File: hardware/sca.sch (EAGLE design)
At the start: 38 parts

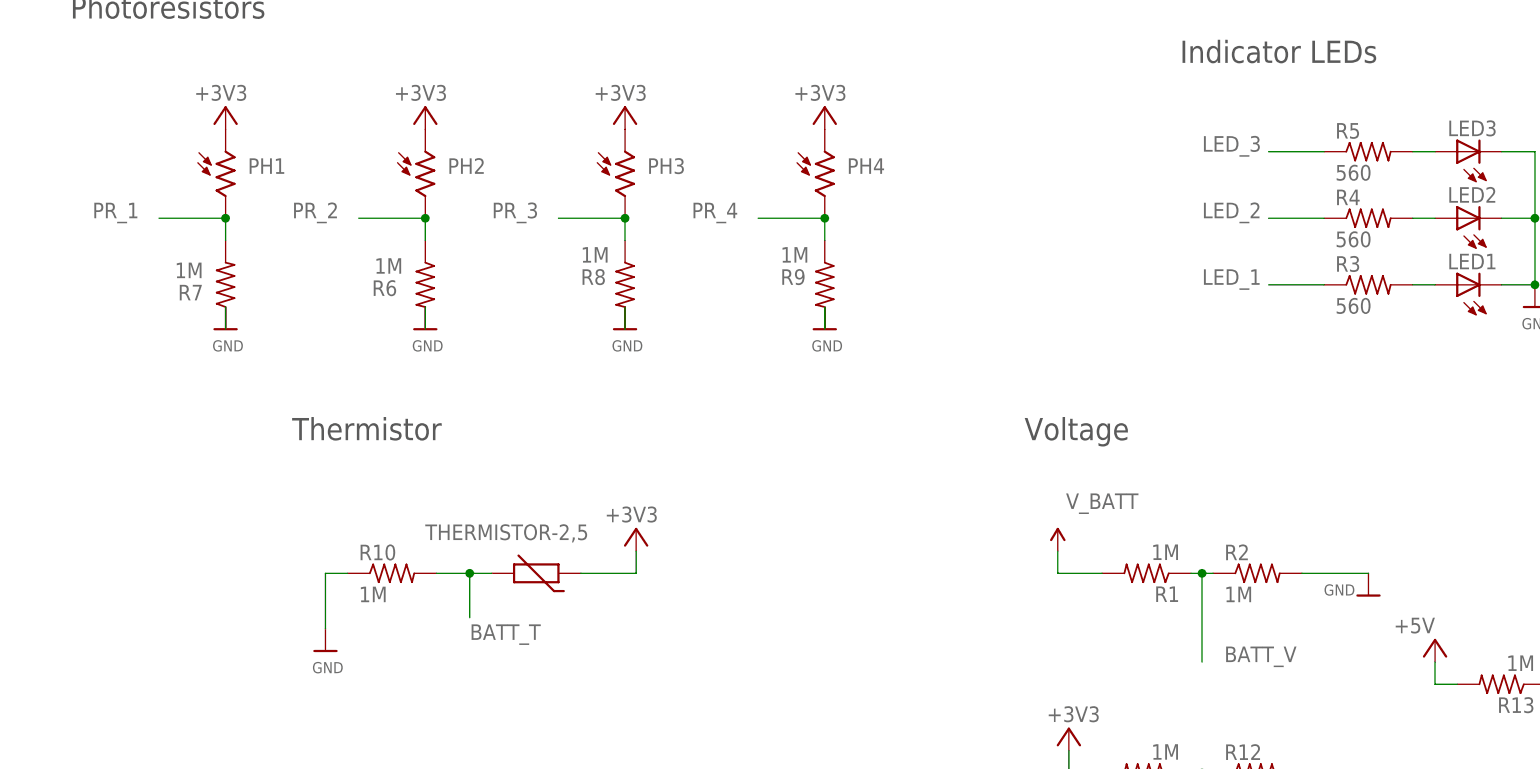
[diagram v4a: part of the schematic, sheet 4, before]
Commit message: updated resistor values
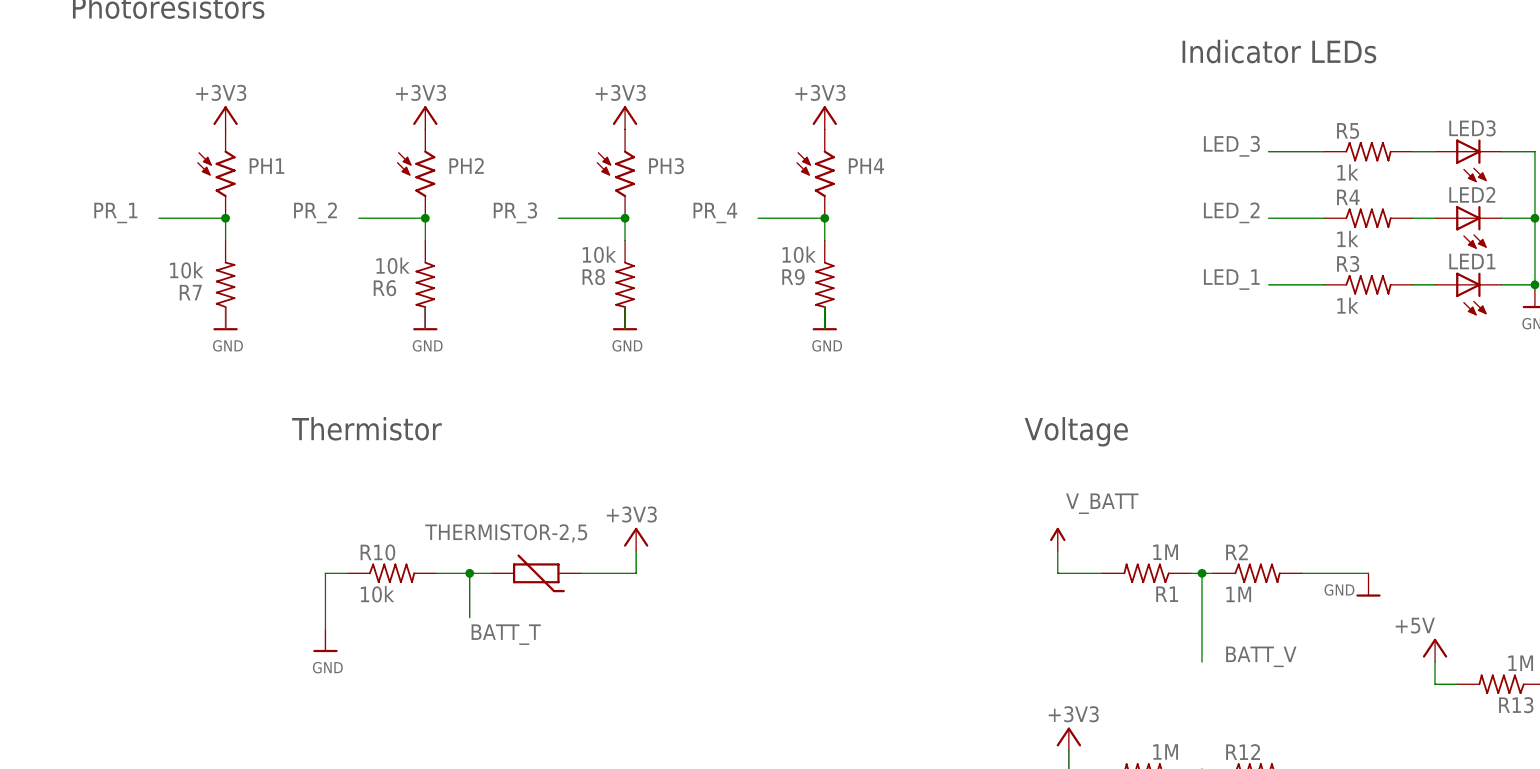
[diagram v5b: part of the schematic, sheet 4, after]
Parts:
- R10, R6, R7, R8, R9: value 1M -> 10k
- R3, R4, R5: value 560 -> 1k
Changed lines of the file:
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@@
 <part name="GPS_H" library="microbuilder" deviceset="HEADER-1X9" device="70MIL"/>
 <part name="P+8" library="supply1" deviceset="+5V" device=""/>
-<part name="R3" library="resistor" library_urn="urn:adsk.eagle:library:348" deviceset="R-US_" device="0309/10" package3d_urn="urn:adsk.eagle:package:23567/1" value="560"/>
-<part name="R4" library="resistor" library_urn="urn:adsk.eagle:library:348" deviceset="R-US_" device="0309/10" package3d_urn="urn:adsk.eagle:package:23567/1" value="560"/>
+<part name="R3" library="resistor" library_urn="urn:adsk.eagle:library:348" deviceset="R-US_" device="0309/10" package3d_urn="urn:adsk.eagle:package:23567/1" value="1k"/>
+<part name="R4" library="resistor" library_urn="urn:adsk.eagle:library:348" deviceset="R-US_" device="0309/10" package3d_urn="urn:adsk.eagle:package:23567/1" value="1k"/>
 <part name="LED1" library="adafruit" library_urn="urn:adsk.eagle:library:420" deviceset="LED" device="3MM" package3d_urn="urn:adsk.eagle:package:6240537/1"/>
 <part name="LED2" library="adafruit" library_urn="urn:adsk.eagle:library:420" deviceset="LED" device="3MM" package3d_urn="urn:adsk.eagle:package:6240537/1"/>
 <part name="LED3" library="adafruit" library_urn="urn:adsk.eagle:library:420" deviceset="LED" device="3MM" package3d_urn="urn:adsk.eagle:package:6240537/1"/>
-<part name="R5" library="resistor" library_urn="urn:adsk.eagle:library:348" deviceset="R-US_" device="0309/10" package3d_urn="urn:adsk.eagle:package:23567/1" value="560"/>
+<part name="R5" library="resistor" library_urn="urn:adsk.eagle:library:348" deviceset="R-US_" device="0309/10" package3d_urn="urn:adsk.eagle:package:23567/1" value="1k"/>
 <part name="U$2" library="microbuilder" deviceset="GND" device=""/>
 <part name="R1" library="resistor" library_urn="urn:adsk.eagle:library:348" deviceset="R-US_" device="0309/10" package3d_urn="urn:adsk.eagle:package:23567/1" value="1M"/>
@@
 <part name="+3V9" library="supply1" deviceset="+3V3" device=""/>
 <part name="+3V10" library="supply1" deviceset="+3V3" device=""/>
-<part name="R6" library="resistor" library_urn="urn:adsk.eagle:library:348" deviceset="R-US_" device="0309/10" package3d_urn="urn:adsk.eagle:package:23567/1" value="1M"/>
-<part name="R7" library="resistor" library_urn="urn:adsk.eagle:library:348" deviceset="R-US_" device="0309/10" package3d_urn="urn:adsk.eagle:package:23567/1" value="1M"/>
-<part name="R8" library="resistor" library_urn="urn:adsk.eagle:library:348" deviceset="R-US_" device="0309/10" package3d_urn="urn:adsk.eagle:package:23567/1" value="1M"/>
-<part name="R9" library="resistor" library_urn="urn:adsk.eagle:library:348" deviceset="R-US_" device="0309/10" package3d_urn="urn:adsk.eagle:package:23567/1" value="1M"/>
-<part name="R10" library="resistor" library_urn="urn:adsk.eagle:library:348" deviceset="R-US_" device="0309/10" package3d_urn="urn:adsk.eagle:package:23567/1" value="1M"/>
+<part name="R6" library="resistor" library_urn="urn:adsk.eagle:library:348" deviceset="R-US_" device="0309/10" package3d_urn="urn:adsk.eagle:package:23567/1" value="10k"/>
+<part name="R7" library="resistor" library_urn="urn:adsk.eagle:library:348" deviceset="R-US_" device="0309/10" package3d_urn="urn:adsk.eagle:package:23567/1" value="10k"/>
+<part name="R8" library="resistor" library_urn="urn:adsk.eagle:library:348" deviceset="R-US_" device="0309/10" package3d_urn="urn:adsk.eagle:package:23567/1" value="10k"/>
+<part name="R9" library="resistor" library_urn="urn:adsk.eagle:library:348" deviceset="R-US_" device="0309/10" package3d_urn="urn:adsk.eagle:package:23567/1" value="10k"/>
+<part name="R10" library="resistor" library_urn="urn:adsk.eagle:library:348" deviceset="R-US_" device="0309/10" package3d_urn="urn:adsk.eagle:package:23567/1" value="10k"/>
 <part name="TEENSY3.6" library="Teensy_3_and_LC_Series_Boards_v1.4" deviceset="TEENSY_3.6_DIL" device=""/>
 <part name="+3V11" library="supply1" deviceset="+3V3" device=""/>

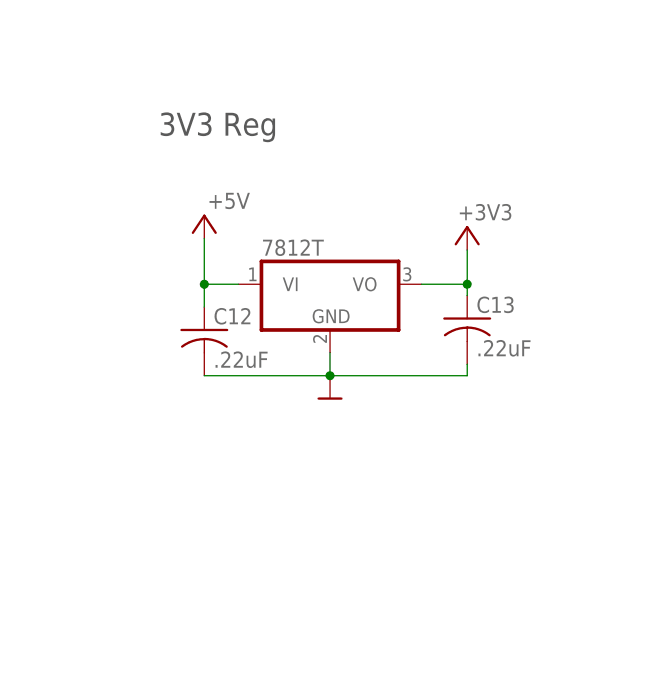
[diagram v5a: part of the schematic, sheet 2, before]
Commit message: updated 3V3 regulator
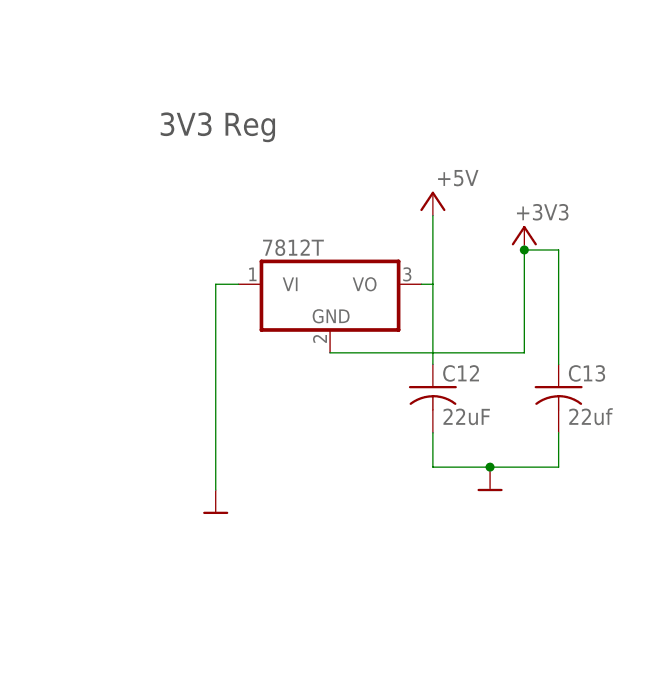
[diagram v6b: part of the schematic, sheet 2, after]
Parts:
- C12: value .22uF -> 22uF
- C13: value .22uF -> 22uf
- R2: value 1M -> 470k
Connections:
- net +3V3: now also 3V3_REG.GND; no longer 3V3_REG.VO
- net +5V: now also 3V3_REG.VO; no longer 3V3_REG.VI
- net GND: now also 3V3_REG.VI; no longer 3V3_REG.GND
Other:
- moved on the sheet: C12, C13
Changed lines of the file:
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@@
 <part name="C10" library="adafruit" library_urn="urn:adsk.eagle:library:420" deviceset="C-US" device="025-040X050" package3d_urn="urn:adsk.eagle:package:6240321/1" value=".22uF"/>
 <part name="C11" library="adafruit" library_urn="urn:adsk.eagle:library:420" deviceset="C-US" device="025-040X050" package3d_urn="urn:adsk.eagle:package:6240321/1" value=".22uF"/>
-<part name="C12" library="adafruit" library_urn="urn:adsk.eagle:library:420" deviceset="C-US" device="025-040X050" package3d_urn="urn:adsk.eagle:package:6240321/1" value=".22uF"/>
-<part name="C13" library="adafruit" library_urn="urn:adsk.eagle:library:420" deviceset="C-US" device="025-040X050" package3d_urn="urn:adsk.eagle:package:6240321/1" value=".22uF"/>
+<part name="C12" library="adafruit" library_urn="urn:adsk.eagle:library:420" deviceset="C-US" device="025-040X050" package3d_urn="urn:adsk.eagle:package:6240321/1" value="22uF"/>
+<part name="C13" library="adafruit" library_urn="urn:adsk.eagle:library:420" deviceset="C-US" device="025-040X050" package3d_urn="urn:adsk.eagle:package:6240321/1" value="22uf"/>
 <part name="P+2" library="supply1" deviceset="+5V" device=""/>
 <part name="+3V2" library="supply1" deviceset="+3V3" device=""/>
@@
 <part name="U$2" library="microbuilder" deviceset="GND" device=""/>
 <part name="R1" library="resistor" library_urn="urn:adsk.eagle:library:348" deviceset="R-US_" device="0309/10" package3d_urn="urn:adsk.eagle:package:23567/1" value="1M"/>
-<part name="R2" library="resistor" library_urn="urn:adsk.eagle:library:348" deviceset="R-US_" device="0309/10" package3d_urn="urn:adsk.eagle:package:23567/1" value="1M"/>
+<part name="R2" library="resistor" library_urn="urn:adsk.eagle:library:348" deviceset="R-US_" device="0309/10" package3d_urn="urn:adsk.eagle:package:23567/1" value="470k"/>
 <part name="U$4" library="microbuilder" deviceset="GND" device=""/>
 <part name="SUPPLY1" library="SparkFun-PowerSymbols" library_urn="urn:adsk.eagle:library:530" deviceset="V_BATT" device=""/>
@@
 <part name="U$14" library="microbuilder" deviceset="GND" device=""/>
 <part name="+5V" library="supply1" deviceset="+5V" device=""/>
+<part name="U$9" library="microbuilder" deviceset="GND" device=""/>
 </parts>
 <sheets>
@@
 <attribute name="VALUE" x="191.77" y="111.125" size="1.778" layer="96"/>
 </instance>
-<instance part="U$10" gate="G$1" x="199.39" y="95.25" smashed="yes" grouprefs="3V3_REGULATOR"/>
-<instance part="C12" gate="G$1" x="185.42" y="102.87" smashed="yes" grouprefs="3V3_REGULATOR">
-<attribute name="NAME" x="186.436" y="103.505" size="1.778" layer="95"/>
-<attribute name="VALUE" x="186.436" y="98.679" size="1.778" layer="96"/>
-</instance>
-<instance part="C13" gate="G$1" x="214.63" y="104.14" smashed="yes" grouprefs="3V3_REGULATOR">
-<attribute name="NAME" x="215.646" y="104.775" size="1.778" layer="95"/>
-<attribute name="VALUE" x="215.646" y="99.949" size="1.778" layer="96"/>
-</instance>
-<instance part="+3V2" gate="G$1" x="214.63" y="114.3" smashed="yes" grouprefs="3V3_REGULATOR">
-<attribute name="VALUE" x="219.71" y="116.84" size="1.778" layer="96" rot="R180"/>
-</instance>
-<instance part="P+3" gate="1" x="185.42" y="115.57" smashed="yes" grouprefs="3V3_REGULATOR">
-<attribute name="VALUE" x="190.5" y="118.11" size="1.778" layer="96" rot="R180"/>
+<instance part="U$10" gate="G$1" x="186.69" y="82.55" smashed="yes" grouprefs="3V3_REGULATOR"/>
+<instance part="C12" gate="G$1" x="210.82" y="96.52" smashed="yes" grouprefs="3V3_REGULATOR">
+<attribute name="NAME" x="211.836" y="97.155" size="1.778" layer="95"/>
+<attribute name="VALUE" x="211.836" y="92.329" size="1.778" layer="96"/>
+</instance>
+<instance part="C13" gate="G$1" x="224.79" y="96.52" smashed="yes" grouprefs="3V3_REGULATOR">
+<attribute name="NAME" x="225.806" y="97.155" size="1.778" layer="95"/>
+<attribute name="VALUE" x="225.806" y="92.329" size="1.778" layer="96"/>
+</instance>
+<instance part="+3V2" gate="G$1" x="220.98" y="114.3" smashed="yes" grouprefs="3V3_REGULATOR">
+<attribute name="VALUE" x="226.06" y="116.84" size="1.778" layer="96" rot="R180"/>
+</instance>
+<instance part="P+3" gate="1" x="210.82" y="118.11" smashed="yes" grouprefs="3V3_REGULATOR">
+<attribute name="VALUE" x="215.9" y="120.65" size="1.778" layer="96" rot="R180"/>
 </instance>
 <instance part="5V_REG" gate="A1" x="128.27" y="105.41" smashed="yes" grouprefs="5V_REGULATOR">
@@
 <attribute name="VALUE" x="63.246" y="92.71" size="1.27" layer="96"/>
 </instance>
+<instance part="U$9" gate="G$1" x="217.17" y="85.09" smashed="yes"/>
 </instances>
 <busses>
@@
 <nets>
 <net name="GND" class="0">
-<segment>
-<pinref part="U$10" gate="G$1" pin="GND"/>
-<pinref part="3V3_REG" gate="A1" pin="GND"/>
-<wire x1="199.39" y1="97.79" x2="199.39" y2="100.33" width="0.1524" layer="91" grouprefs="3V3_REGULATOR"/>
-<pinref part="C12" gate="G$1" pin="2"/>
-<wire x1="185.42" y1="97.79" x2="199.39" y2="97.79" width="0.1524" layer="91" grouprefs="3V3_REGULATOR"/>
-<junction x="199.39" y="97.79" grouprefs="3V3_REGULATOR"/>
-<pinref part="C13" gate="G$1" pin="2"/>
-<wire x1="214.63" y1="99.06" x2="214.63" y2="97.79" width="0.1524" layer="91" grouprefs="3V3_REGULATOR"/>
-<wire x1="214.63" y1="97.79" x2="199.39" y2="97.79" width="0.1524" layer="91" grouprefs="3V3_REGULATOR"/>
-</segment>
 <segment>
 <pinref part="U$3" gate="G$1" pin="GND"/>
@@
 <wire x1="64.77" y1="99.06" x2="64.77" y2="97.79" width="0.1524" layer="91" grouprefs="BATT_CONNECTOR"/>
 </segment>
-</net>
-<net name="+3V3" class="0">
-<segment>
-<pinref part="3V3_REG" gate="A1" pin="VO"/>
-<pinref part="C13" gate="G$1" pin="1"/>
-<wire x1="209.55" y1="107.95" x2="214.63" y2="107.95" width="0.1524" layer="91" grouprefs="3V3_REGULATOR"/>
-<wire x1="214.63" y1="107.95" x2="214.63" y2="106.68" width="0.1524" layer="91" grouprefs="3V3_REGULATOR"/>
-<pinref part="+3V2" gate="G$1" pin="+3V3"/>
-<wire x1="214.63" y1="107.95" x2="214.63" y2="111.76" width="0.1524" layer="91" grouprefs="3V3_REGULATOR"/>
-<junction x="214.63" y="107.95" grouprefs="3V3_REGULATOR"/>
+<segment>
+<pinref part="U$10" gate="G$1" pin="GND"/>
+<pinref part="3V3_REG" gate="A1" pin="VI"/>
+<wire x1="186.69" y1="85.09" x2="186.69" y2="107.95" width="0.1524" layer="91"/>
+<wire x1="186.69" y1="107.95" x2="189.23" y2="107.95" width="0.1524" layer="91"/>
+</segment>
+<segment>
+<pinref part="C13" gate="G$1" pin="2"/>
+<pinref part="U$9" gate="G$1" pin="GND"/>
+<wire x1="224.79" y1="91.44" x2="224.79" y2="87.63" width="0.1524" layer="91"/>
+<wire x1="224.79" y1="87.63" x2="217.17" y2="87.63" width="0.1524" layer="91"/>
+<pinref part="C12" gate="G$1" pin="2"/>
+<wire x1="217.17" y1="87.63" x2="210.82" y2="87.63" width="0.1524" layer="91"/>
+<wire x1="210.82" y1="87.63" x2="210.82" y2="91.44" width="0.1524" layer="91"/>
+<junction x="217.17" y="87.63"/>
 </segment>
 </net>
 <net name="+5V" class="0">
-<segment>
-<pinref part="C12" gate="G$1" pin="1"/>
-<pinref part="3V3_REG" gate="A1" pin="VI"/>
-<wire x1="185.42" y1="105.41" x2="185.42" y2="107.95" width="0.1524" layer="91" grouprefs="3V3_REGULATOR"/>
-<wire x1="185.42" y1="107.95" x2="189.23" y2="107.95" width="0.1524" layer="91" grouprefs="3V3_REGULATOR"/>
-<pinref part="P+3" gate="1" pin="+5V"/>
-<wire x1="185.42" y1="113.03" x2="185.42" y2="107.95" width="0.1524" layer="91" grouprefs="3V3_REGULATOR"/>
-<junction x="185.42" y="107.95" grouprefs="3V3_REGULATOR"/>
-</segment>
 <segment>
 <pinref part="C11" gate="G$1" pin="1"/>
@@
 <wire x1="143.51" y1="105.41" x2="143.51" y2="109.22" width="0.1524" layer="91" grouprefs="5V_REGULATOR"/>
 </segment>
+<segment>
+<pinref part="P+3" gate="1" pin="+5V"/>
+<pinref part="3V3_REG" gate="A1" pin="VO"/>
+<wire x1="210.82" y1="115.57" x2="210.82" y2="107.95" width="0.1524" layer="91"/>
+<wire x1="210.82" y1="107.95" x2="209.55" y2="107.95" width="0.1524" layer="91"/>
+<wire x1="210.82" y1="107.95" x2="210.82" y2="99.06" width="0.1524" layer="91"/>
+<pinref part="C12" gate="G$1" pin="1"/>
+</segment>
 </net>
 <net name="V_BATT" class="0">
@@
 </segment>
 </net>
+<net name="+3V3" class="0">
+<segment>
+<pinref part="3V3_REG" gate="A1" pin="GND"/>
+<wire x1="199.39" y1="100.33" x2="220.98" y2="100.33" width="0.1524" layer="91"/>
+<pinref part="+3V2" gate="G$1" pin="+3V3"/>
+<wire x1="220.98" y1="111.76" x2="220.98" y2="100.33" width="0.1524" layer="91"/>
+<pinref part="C13" gate="G$1" pin="1"/>
+<wire x1="224.79" y1="99.06" x2="224.79" y2="111.76" width="0.1524" layer="91"/>
+<wire x1="224.79" y1="111.76" x2="220.98" y2="111.76" width="0.1524" layer="91"/>
+<junction x="220.98" y="111.76"/>
+</segment>
+</net>
